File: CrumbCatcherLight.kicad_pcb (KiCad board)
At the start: 2 copper layers, 79.8 x 72.4 mm, 78 parts, among them J1 USB_C_Receptacle, J2 Conn_ARM_SWD_TagConnect_TC203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, Q1 2N7002VC-7, SW1 TL3780AF240QG, SW10 SW_SPST, SW11 PEC11R, SW12 PEC11R, SW13 PEC11R, SW2 SW_SPST, SW3 SW_SPST, SW4 SW_SPST, SW5 SW_SPST, SW6 SW_SPST, SW7 SW_SPST, SW8 SW_SPST, SW9 SW_SPST, U1 ECMF02-2AMX6, U2 PCB, U3 XC6210B332MR, U4 GD25LQ128DYIGR, U5 RP2040, Y1 12MHz

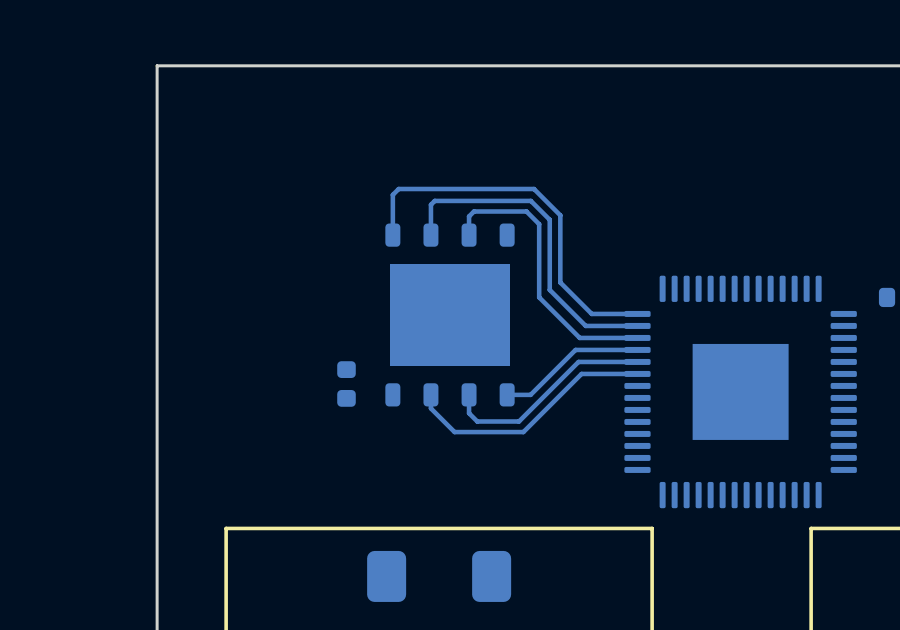
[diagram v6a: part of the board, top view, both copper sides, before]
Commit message: add footprint for flash and 3d model
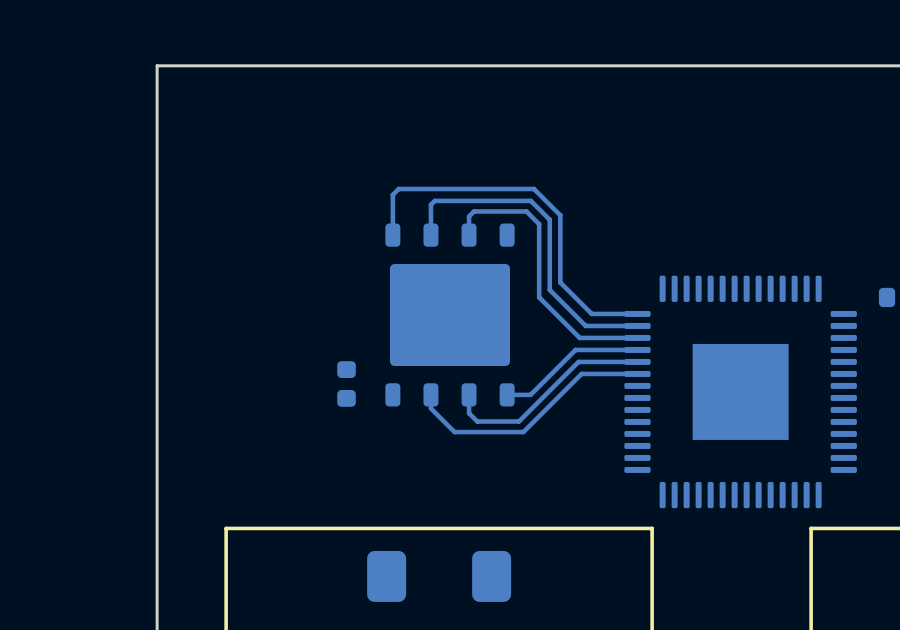
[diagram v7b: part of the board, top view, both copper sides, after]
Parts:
- U4: value GD25LQ128DYIGR -> GD25Q127CWIGR; footprint Package_SON:WSON-8-1EP_6x5mm_P1.27mm_EP3.4x4mm -> Mad_Footprints:GD25LQ128DYIGR
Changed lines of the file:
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@@
 		)
 	)
-	(footprint "Package_SON:WSON-8-1EP_6x5mm_P1.27mm_EP3.4x4mm"
+	(footprint "Mad_Footprints:GD25LQ128DYIGR"
 		(layer "B.Cu")
 		(at 111.3625 77.285 -90)
-		(descr "WSON, 8 Pin (http://ww1.microchip.com/downloads/en/AppNotes/S72030.pdf), generated with kicad-footprint-generator ipc_noLead_generator.py")
-		(tags "WSON NoLead")
+		(descr "WSON, 8 Pin (https://www.gigadevice.com.cn/Public/Uploads/uploadfile/files/20220714/DS-00291-GD25LQ128D-Rev1.9.pdf)")
+		(tags "WSON NoLead GD25LQ128")
 		(property "Reference" "U4"
-			(at 0 3.45 90)
+			(at 0 3.45 -90)
 			(layer "B.SilkS")
 			(effects
@@
 			)
 		)
-		(property "Value" "GD25LQ128DYIGR"
-			(at 0 -3.45 90)
-			(layer "B.Fab")
-			(effects
-				(font
-					(size 1 1)
-					(thickness 0.15)
-				)
-				(justify mirror)
-			)
-		)
-		(property "Footprint" "Package_SON:WSON-8-1EP_6x5mm_P1.27mm_EP3.4x4mm"
+		(property "Value" "GD25Q127CWIGR"
+			(at 0 -3.45 -90)
+			(layer "B.Fab")
+			(effects
+				(font
+					(size 1 1)
+					(thickness 0.15)
+				)
+				(justify mirror)
+			)
+		)
+		(property "Footprint" "Mad_Footprints:GD25LQ128DYIGR"
 			(at 0 0 90)
 			(unlocked yes)
@@
 			)
 		)
-		(property "Description" "FLASH - NOR Memory IC 128Mbit SPI - Quad I/O 120 MHz 8-WSON (6x8)"
+		(property "Description" "FLASH - NOR Memory IC 128Mbit SPI - Quad I/O 104 MHz 8-WSON (5x6)"
 			(at 0 0 90)
 			(unlocked yes)
@@
 			)
 		)
-		(property "Supplier PN" "1970-1088-1-ND"
-			(at 0 0 90)
-			(unlocked yes)
-			(layer "B.Fab")
-			(hide yes)
-			(effects
-				(font
-					(size 1 1)
-					(thickness 0.15)
-				)
-				(justify mirror)
-			)
-		)
-		(property "MPN" "GD25LQ128DYIGR"
+		(property "Supplier PN" "1970-1048-1-ND"
+			(at 0 0 90)
+			(unlocked yes)
+			(layer "B.Fab")
+			(hide yes)
+			(effects
+				(font
+					(size 1 1)
+					(thickness 0.15)
+				)
+				(justify mirror)
+			)
+		)
+		(property "MPN" "GD25Q127CWIGR"
 			(at 0 0 90)
 			(unlocked yes)
@@
 		)
 		(fp_text user "${REFERENCE}"
-			(at 0 0 90)
+			(at 0 0 -90)
 			(layer "B.Fab")
 			(effects
@@
 			(pintype "power_in")
 		)
-		(pad "9" smd rect
+		(pad "9" smd roundrect
 			(at 0 0 270)
 			(size 3.4 4)
 			(property pad_prop_heatsink)
 			(layers "B.Cu" "B.Mask")
+			(roundrect_rratio 0.04411764706)
 			(net 11 "GND")
 			(pinfunction "GND")
@@
 			(zone_connect 2)
 		)
-		(model "${KICAD8_3DMODEL_DIR}/Package_SON.3dshapes/WSON-8-1EP_6x5mm_P1.27mm_EP3.4x4mm.wrl"
+		(model "${KIPRJMOD}/mad_lib/part_library/models/GigaDevice Semiconductor (HK) Limited/GD25LQ128DYIGR.step"
 			(offset
 				(xyz 0 0 0)
@@
 			)
 			(rotate
-				(xyz 0 0 0)
-			)
-		)
+				(xyz -90 0 0)
+			)
+		)

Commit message: Refactor, cleanup, add todo list, update metadata on BOM
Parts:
- removed C22, C23, C24, C25: 100nF, Capacitor_SMD:C_0402_1005Metric
- removed D11, D12, D13: LL4148, Diode_SMD:D_MiniMELF
- removed SW12, SW13: PEC11R, Mad_Footprints:RotaryEncoder_Bourns_Vertical_PEC12R-3x17F-Sxxxx
- removed SW8: SW_SPST, Mad_Footprints:SW_Hotswap_Kailh_MX_1.00u
- added C26: 100nF, Capacitor_SMD:C_0402_1005Metric, B.Cu at (174.1, 79.5)
- added C27: 100nF, Capacitor_SMD:C_0402_1005Metric, B.Cu at (174.1, 81.5)
- added C28: 100nF, Capacitor_SMD:C_0402_1005Metric, B.Cu at (174.1, 83.5)
- added C29: 100nF, Capacitor_SMD:C_0402_1005Metric, B.Cu at (174.1, 85.4)
- C7: footprint Capacitor_SMD:C_0402_1005Metric -> Capacitor_SMD:C_0805_2012Metric
- D2, D5, D8: moved to F.Cu
- SW2, SW5: value SW_SPST -> PEC11R; footprint Mad_Footprints:SW_Hotswap_Kailh_MX_1.00u -> Mad_Footprints:RotaryEncoder_Bourns_Vertical_PEC12R-3x17F-Sxxxx
- moved C20 104.9 mm to (173.9, 74.5)
- moved C21 104.9 mm to (173.9, 76.5)
- moved C5 85.8 mm to (53.9, 45.4)
- moved C7 85.8 mm to (43.3, 32.6)
- moved R4 85.8 mm to (51.3, 49.5)
- moved TP1 85.8 mm to (14.4, 53.2)
- moved TP2 85.8 mm to (14.4, 56.2)
- moved TP3 85.8 mm to (14.4, 59.3)
- moved Q1 85.0 mm to (51.5, 38.5)
- moved R3 83.5 mm to (46.9, 42.3)
- moved R7 83.5 mm to (44.1, 40.0)
- moved R8 83.5 mm to (44.1, 41.9)
- moved R6 82.9 mm to (51.0, 40.4)
- moved D1 79.0 mm to (51.0, 35.4)
- moved R5 78.1 mm to (51.3, 36.6), turned to 180 degrees
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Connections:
- C1 pad 2: GND -> /PreFIlterGND
- C20 pad 1: /RP2040/GPIO11 -> /RP2040/GPIO15
- C21 pad 2: /RP2040/GPIO12 -> /RP2040/GPIO16
- SW11 pad A: /RP2040/GPIO11 -> /RP2040/GPIO15
- SW11 pad B: /RP2040/GPIO12 -> /RP2040/GPIO16
- SW11 pad S1: /RP2040/GPIO10 -> /RP2040/GPIO9
- SW11 pad S2: Net-(D11-A) -> Net-(D8-A)
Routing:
- net /RP2040/QSPI_nCS: track 12.6 -> 0.00 mm
- net /RP2040/QSPI_SD1: track 11.0 -> 0.00 mm
- net /RP2040/QSPI_SD2: track 9.48 -> 0.00 mm
- net /RP2040/QSPI_SD3: track 8.47 -> 0.00 mm
- net Net-(U5-XTAL_IN): track 0.00 -> 8.23 mm
- net /RP2040/QSPI_SCLK: track 7.16 -> 0.00 mm
- net /RP2040/QSPI_SD0: track 4.97 -> 0.00 mm
- net Net-(C15-Pad2): track 0.00 -> 2.89 mm
- net GND: track 3.33 -> 6.16 mm
- net Net-(U1-D+_in): track 0.00 -> 2.38 mm
- net Net-(U1-D-_in): track 0.00 -> 2.38 mm
- net Net-(U5-XTAL_OUT): track 0.00 -> 1.93 mm
- net Net-(J1-CC1): track 0.00 -> 1.59 mm
- net Net-(J1-CC2): track 0.00 -> 1.50 mm
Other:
- board size 79.8 x 72.4 mm -> 60.1 x 69.1 mm
